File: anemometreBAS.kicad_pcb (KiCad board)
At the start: 2 copper layers, 1 part

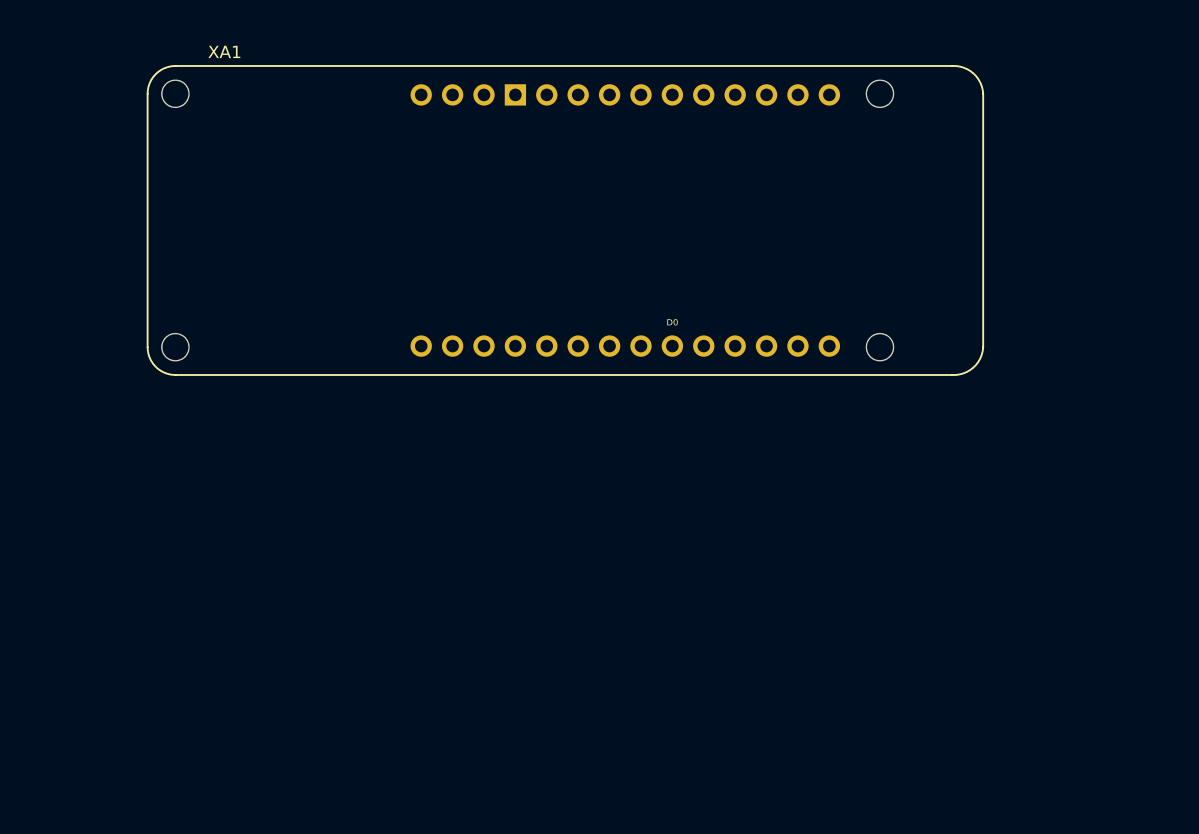
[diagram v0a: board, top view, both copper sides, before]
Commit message: first pcb version with schematic footprint update
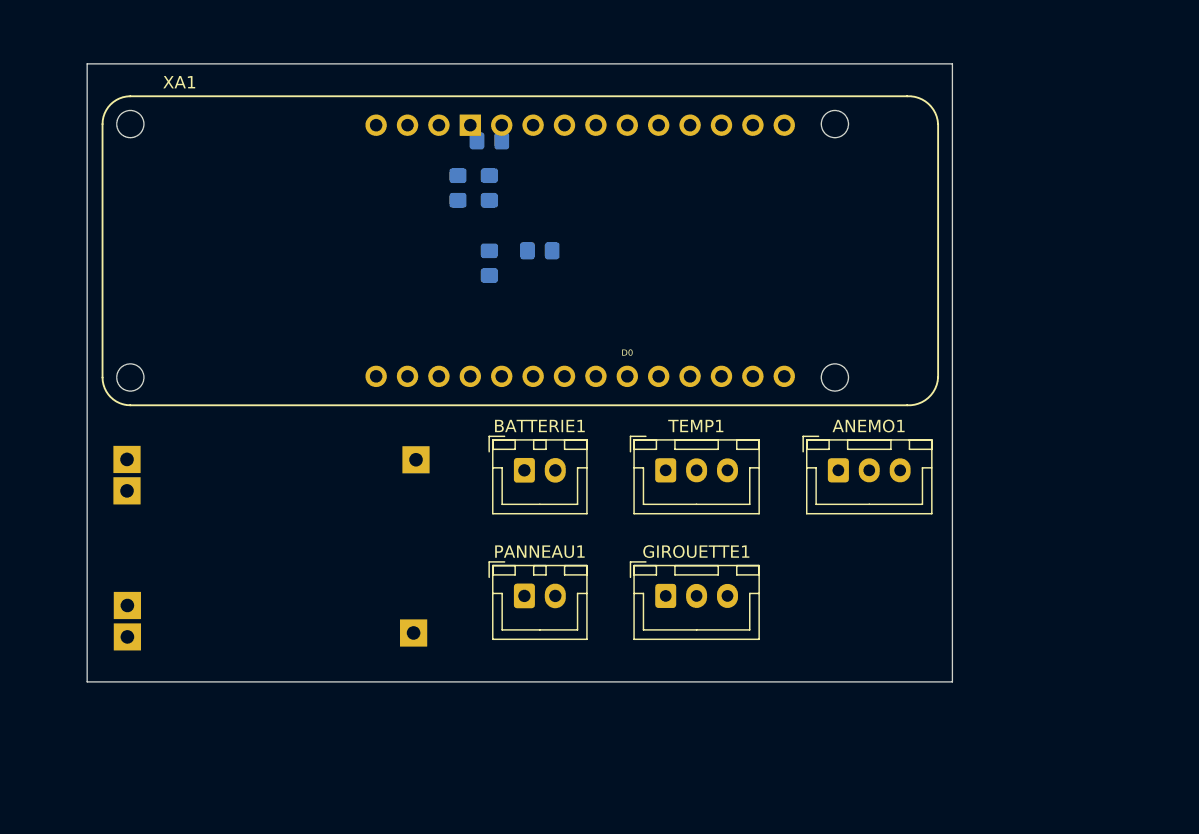
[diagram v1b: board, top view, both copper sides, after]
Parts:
- added ANEMO1: Conn_01x02_Male, Connector_JST:JST_XH_B3B-XH-A_1x03_P2.50mm_Vertical, F.Cu at (157.8, 88.9)
- added BATTERIE1: Conn_01x02_Male, Connector_JST:JST_XH_B2B-XH-A_1x02_P2.50mm_Vertical, F.Cu at (132.4, 88.9)
- added GIROUETTE1: Conn_01x02_Male, Connector_JST:JST_XH_B3B-XH-A_1x03_P2.50mm_Vertical, F.Cu at (143.8, 99.0)
- added PANNEAU1: Conn_01x02_Male, Connector_JST:JST_XH_B2B-XH-A_1x02_P2.50mm_Vertical, F.Cu at (132.4, 99.0)
- added R1: 4.7K, Resistor_SMD:R_0805_2012Metric_Pad1.20x1.40mm_HandSolder, B.Cu at (129.5, 72.1)
- added R2: 10K, Resistor_SMD:R_0805_2012Metric_Pad1.20x1.40mm_HandSolder, B.Cu at (133.6, 71.1)
- added R3: 10K, Resistor_SMD:R_0805_2012Metric_Pad1.20x1.40mm_HandSolder, B.Cu at (129.5, 66.0)
- added R4: 1.5K, Resistor_SMD:R_0805_2012Metric_Pad1.20x1.40mm_HandSolder, B.Cu at (127.0, 66.0)
- added R5: 2.5K, Resistor_SMD:R_0805_2012Metric_Pad1.20x1.40mm_HandSolder, B.Cu at (129.5, 62.2)
- added TEMP1: Conn_01x03_Male, Connector_JST:JST_XH_B3B-XH-A_1x03_P2.50mm_Vertical, F.Cu at (143.8, 88.9)
- added U1: TP4056, TP4056:TP4056, B.Cu at (125.0, 103.6)
- moved XA1 4.39 mm to (100.5, 60.9)
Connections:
- XA1 pad 3V3: unconnected-(XA1-Pad3V3) -> 3V3
- XA1 pad 5V: unconnected-(XA1-Pad5V) -> 5V
- XA1 pad A1: unconnected-(XA1-PadA1) -> Net-(TEMP1-Pad1)
- XA1 pad A4: unconnected-(XA1-PadA4) -> VBridgeBat
- XA1 pad A6: unconnected-(XA1-PadA6) -> VBridgeDir
- XA1 pad D0: unconnected-(XA1-PadD0) -> Net-(ANEMO1-Pad2)
- XA1 pad GND: unconnected-(XA1-PadGND) -> GND
- XA1 pad VIN: unconnected-(XA1-PadVIN) -> VIN
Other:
- board outline added: 70 x 50 mm

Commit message: schematic 	GND at the same pin for each connector 	add M3 hole*3 connected to GND PCB 	first routing
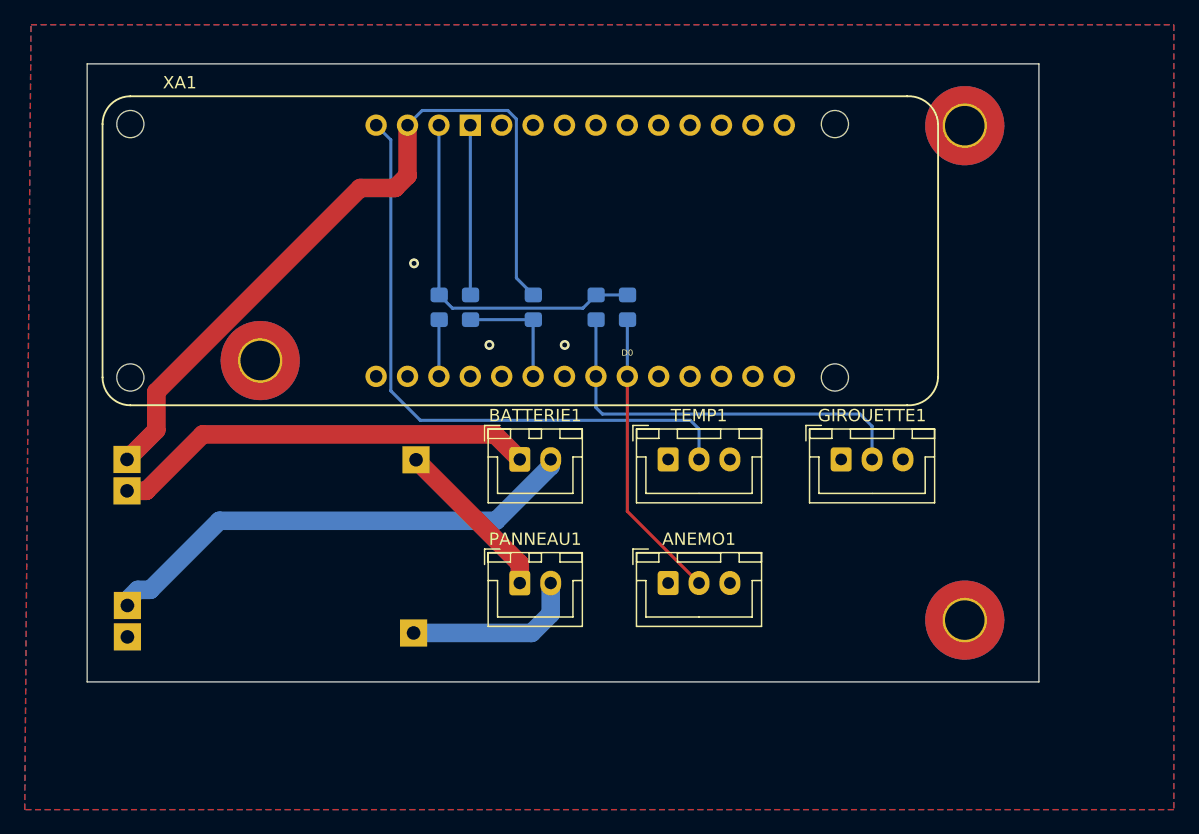
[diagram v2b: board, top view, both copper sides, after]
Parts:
- added H2: MountingHole_Pad, MountingHole:MountingHole_3.2mm_M3_Pad_TopBottom, F.Cu at (168.0, 101.0)
- added H3: MountingHole_Pad, MountingHole:MountingHole_3.2mm_M3_Pad_TopBottom, F.Cu at (168.0, 61.0)
- added H4: MountingHole_Pad, MountingHole:MountingHole_3.2mm_M3_Pad_TopBottom, F.Cu at (111.0, 80.0)
- moved GIROUETTE1 18.0 mm to (158.0, 88.0)
- moved ANEMO1 16.5 mm to (144.0, 98.0)
- moved R5 13.5 mm to (128.0, 75.7), turned to 90 degrees
- moved R3 13.0 mm to (138.2, 75.7)
- moved R4 11.4 mm to (133.1, 75.7)
- moved R2 8.44 mm to (140.7, 75.7), turned to 90 degrees
- moved R1 5.41 mm to (125.5, 75.7)
- moved PANNEAU1 1.11 mm to (132.0, 98.0)
- moved BATTERIE1 0.96 mm to (132.0, 88.0)
- moved TEMP1 0.90 mm to (144.0, 88.0)
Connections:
- GIROUETTE1 pad 1: VBridgeDir -> GND
- GIROUETTE1 pad 2: GND -> VBridgeDir
- R1 pad 2: Net-(TEMP1-Pad1) -> Net-(TEMP1-Pad3)
- TEMP1 pad 1: Net-(TEMP1-Pad1) -> GND
- TEMP1 pad 3: GND -> Net-(TEMP1-Pad3)
- XA1 pad A1: Net-(TEMP1-Pad1) -> Net-(TEMP1-Pad3)
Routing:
- net VIN: track 0.00 -> 62.5 mm
- net 5V: track 0.00 -> 50.7 mm
- net Net-(BATTERIE1-Pad2): track 0.00 -> 39.7 mm
- net Net-(BATTERIE1-Pad1): track 0.00 -> 34.5 mm
- net VBridgeDir: track 0.00 -> 33.5 mm
- net 3V3: track 0.00 -> 29.9 mm
- net Net-(ANEMO1-Pad2): track 0.00 -> 23.7 mm
- net Net-(PANNEAU1-Pad2): track 0.00 -> 14.2 mm
- net GND: track 0.00 -> 13.7 mm, vias 0 -> 3
- net Net-(PANNEAU1-Pad1): track 0.00 -> 13.5 mm
- net VBridgeBat: track 0.00 -> 9.68 mm
- net Net-(TEMP1-Pad3): track 0.00 -> 5.24 mm
- added copper zone on B.Cu, net GND
- added copper zone on F.Cu, net GND
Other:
- board size 70 x 50 mm -> 77 x 50 mm

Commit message: route temp sensor data change +5V net location change hole location drc ok only one error with hole under mkr processing board
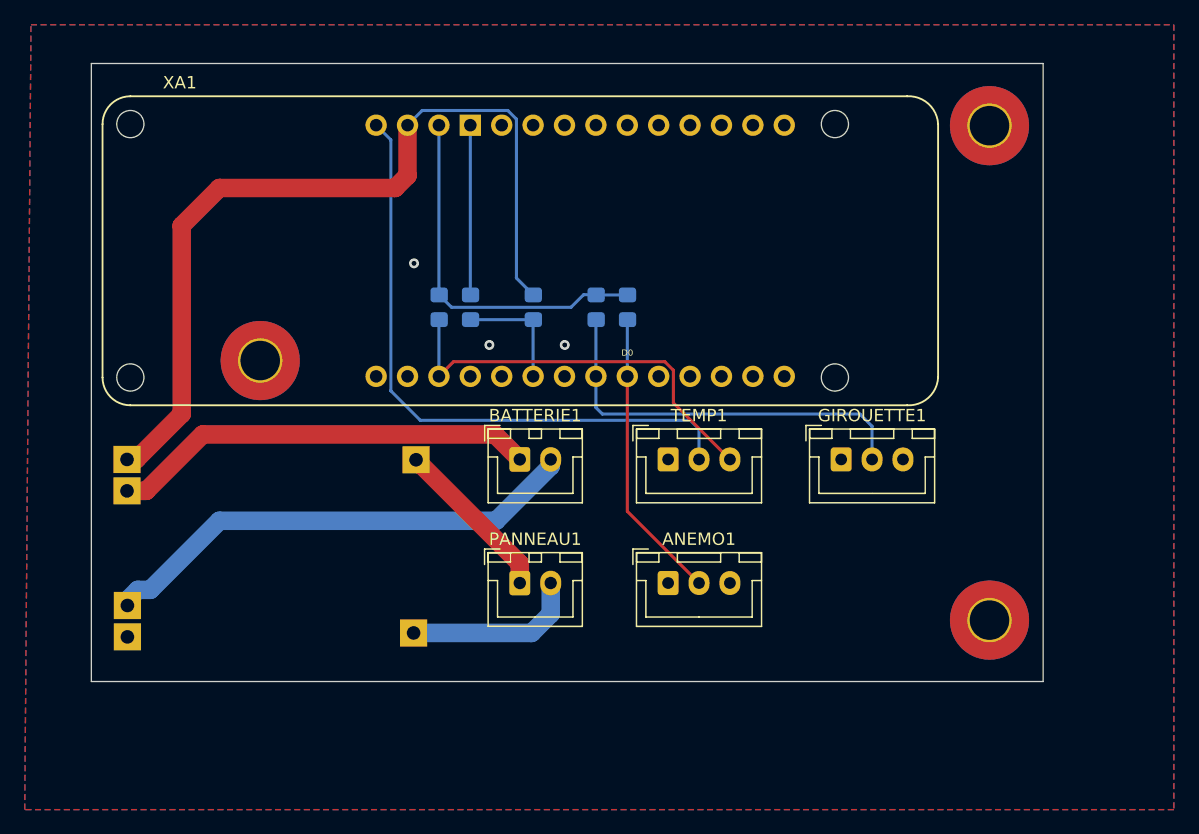
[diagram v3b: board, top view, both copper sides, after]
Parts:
- moved H2 2.00 mm to (170.0, 101.0)
- moved H3 2.00 mm to (170.0, 61.0)
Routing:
- net Net-(TEMP1-Pad3): track 5.24 -> 33.5 mm
- net VIN: track 62.5 -> 69.6 mm
- net VBridgeDir: track 33.5 -> 32.8 mm
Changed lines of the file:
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@@
   )
   (footprint "MountingHole:MountingHole_3.2mm_M3_Pad_TopBottom" (layer "F.Cu")
-    (at 168 61)
+    (at 170 61)
     (descr "Mounting Hole 3.2mm, M3")
     (tags "mounting hole 3.2mm m3")
@@
   )
   (footprint "MountingHole:MountingHole_3.2mm_M3_Pad_TopBottom" (layer "F.Cu")
-    (at 168 101)
+    (at 170 101)
     (descr "Mounting Hole 3.2mm, M3")
     (tags "mounting hole 3.2mm m3")
@@
       (net 9 "GND") (pinfunction "OUT-") (pintype "output"))
   )
-  (gr_line (start 97 56) (end 174 56) (layer "Edge.Cuts") (width 0.1))
-  (gr_line (start 174 106) (end 174 56) (layer "Edge.Cuts") (width 0.1))
-  (gr_line (start 97 106) (end 97 56) (layer "Edge.Cuts") (width 0.1))
-  (gr_line (start 174 106) (end 97 106) (layer "Edge.Cuts") (width 0.1))
-  (dimension (type aligned) (layer "Edge.Cuts")
-    (pts (xy 174 56) (xy 174 106))
+  (gr_line (start 97.3392 55.9688) (end 174.3392 55.9688) (layer "Edge.Cuts") (width 0.1))
+  (gr_line (start 174.3392 105.9688) (end 174.3392 55.9688) (layer "Edge.Cuts") (width 0.1))
+  (gr_line (start 97.3392 105.9688) (end 97.3392 55.9688) (layer "Edge.Cuts") (width 0.1))
+  (gr_line (start 174.3392 105.9688) (end 97.3392 105.9688) (layer "Edge.Cuts") (width 0.1))
+  (dimension (type aligned) (layer "Cmts.User")
+    (pts (xy 174.3392 55.9688) (xy 174.3392 105.9688))
     (height -8.89)
-    (gr_text "50,0000 mm" (at 181.74 81 90) (layer "Edge.Cuts")
+    (gr_text "50,0000 mm" (at 182.0792 80.9688 90) (layer "Cmts.User")
       (effects (font (size 1 1) (thickness 0.15)))
     )
@@
     (style (thickness 0.1) (arrow_length 1.27) (text_position_mode 0) (extension_height 0.58642) (extension_offset 0.5) keep_text_aligned)
   )
-  (dimension (type aligned) (layer "Edge.Cuts")
-    (pts (xy 174 106) (xy 97 106))
+  (dimension (type aligned) (layer "Cmts.User")
+    (pts (xy 174.3392 105.9688) (xy 97.3392 105.9688))
     (height -6.35)
-    (gr_text "77,0000 mm" (at 135.5 111.2) (layer "Edge.Cuts")
+    (gr_text "77,0000 mm" (at 135.8392 111.1688) (layer "Cmts.User")
       (effects (font (size 1 1) (thickness 0.15)))
     )
@@
   )
   (segment (start 125.4578 74.6738) (end 125.476 74.692) (width 0.25) (layer "B.Cu") (net 1))
-  (segment (start 137.10052 75.76748) (end 138.176 74.692) (width 0.25) (layer "B.Cu") (net 1))
-  (segment (start 137.668 74.692) (end 137.684 74.708) (width 0.25) (layer "B.Cu") (net 1))
-  (segment (start 125.476 74.692) (end 126.55148 75.76748) (width 0.25) (layer "B.Cu") (net 1))
+  (segment (start 136.144 75.692) (end 126.476 75.692) (width 0.25) (layer "B.Cu") (net 1))
+  (segment (start 137.16 74.676) (end 136.144 75.692) (width 0.25) (layer "B.Cu") (net 1))
+  (segment (start 126.476 75.692) (end 125.476 74.692) (width 0.25) (layer "B.Cu") (net 1))
   (segment (start 125.476 74.708) (end 125.4578 74.6898) (width 0.25) (layer "B.Cu") (net 1))
+  (segment (start 138.176 74.692) (end 138.16 74.676) (width 0.25) (layer "B.Cu") (net 1))
   (segment (start 125.4578 60.96) (end 125.4578 74.6738) (width 0.25) (layer "B.Cu") (net 1))
+  (segment (start 138.16 74.676) (end 137.16 74.676) (width 0.25) (layer "B.Cu") (net 1))
   (segment (start 140.716 74.692) (end 138.176 74.692) (width 0.25) (layer "B.Cu") (net 1))
-  (segment (start 126.55148 75.76748) (end 137.10052 75.76748) (width 0.25) (layer "B.Cu") (net 1))
-  (segment (start 102.592521 85.635189) (end 102.592521 82.539183) (width 1.5) (layer "F.Cu") (net 5))
-  (segment (start 102.592521 82.539183) (end 119.091704 66.04) (width 1.5) (layer "F.Cu") (net 5))
-  (segment (start 119.091704 66.04) (end 121.92 66.04) (width 1.5) (layer "F.Cu") (net 5))
-  (segment (start 121.92 66.04) (end 122.9178 65.0422) (width 1.5) (layer "F.Cu") (net 5))
-  (segment (start 122.9178 65.0422) (end 122.9178 60.96) (width 1.5) (layer "F.Cu") (net 5))
-  (segment (start 100.224054 88.003656) (end 102.592521 85.635189) (width 1.5) (layer "F.Cu") (net 5))
+  (segment (start 122.9178 60.96) (end 122.9178 65.0422) (width 1.5) (layer "F.Cu") (net 5))
+  (segment (start 104.648 84.328) (end 100.972344 88.003656) (width 1.5) (layer "F.Cu") (net 5))
+  (segment (start 100.972344 88.003656) (end 100.224054 88.003656) (width 1.5) (layer "F.Cu") (net 5))
+  (segment (start 122.9178 65.0422) (end 121.92 66.04) (width 1.5) (layer "F.Cu") (net 5))
+  (segment (start 121.92 66.04) (end 107.696 66.04) (width 1.5) (layer "F.Cu") (net 5))
+  (segment (start 107.696 66.04) (end 104.648 69.088) (width 1.5) (layer "F.Cu") (net 5))
+  (segment (start 104.648 69.088) (end 104.648 84.328) (width 1.5) (layer "F.Cu") (net 5))
   (segment (start 131.725911 73.321911) (end 131.725911 60.467867) (width 0.25) (layer "B.Cu") (net 5))
   (segment (start 124.105911 59.771889) (end 122.9178 60.96) (width 0.25) (layer "B.Cu") (net 5))
@@
   (segment (start 159.512 84.328) (end 138.684 84.328) (width 0.25) (layer "B.Cu") (net 26))
   (segment (start 160.5 85.316) (end 159.512 84.328) (width 0.25) (layer "B.Cu") (net 26))
-  (segment (start 137.668 76.692) (end 138.1578 77.1818) (width 0.25) (layer "B.Cu") (net 26))
   (segment (start 140.6978 92.1978) (end 140.6978 81.28) (width 0.25) (layer "F.Cu") (net 27))
   (segment (start 146.5 98) (end 140.6978 92.1978) (width 0.25) (layer "F.Cu") (net 27))
@@
   (segment (start 132.962 102.038) (end 123.409 102.038) (width 1.5) (layer "B.Cu") (net 31))
   (segment (start 134.5 98) (end 134.5 100.5) (width 1.5) (layer "B.Cu") (net 31))
+  (segment (start 143.729933 80.091889) (end 126.645911 80.091889) (width 0.25) (layer "F.Cu") (net 32))
+  (segment (start 149 88) (end 144.425911 83.425911) (width 0.25) (layer "F.Cu") (net 32))
+  (segment (start 144.425911 83.425911) (end 144.425911 80.787867) (width 0.25) (layer "F.Cu") (net 32))
+  (segment (start 144.425911 80.787867) (end 143.729933 80.091889) (width 0.25) (layer "F.Cu") (net 32))
+  (segment (start 126.645911 80.091889) (end 125.4578 81.28) (width 0.25) (layer "F.Cu") (net 32))
   (segment (start 125.4578 76.7102) (end 125.4578 81.28) (width 0.25) (layer "B.Cu") (net 32))
-  (segment (start 125.238507 81.060707) (end 125.4578 81.28) (width 0.25) (layer "B.Cu") (net 32))
   (segment (start 125.476 76.692) (end 125.4578 76.7102) (width 0.25) (layer "B.Cu") (net 32))
-  (segment (start 125.476 76.708) (end 125.238507 76.945493) (width 0.25) (layer "B.Cu") (net 32))
   (zone (net 9) (net_name "GND") (layers F&B.Cu) (hatch edge 0.508)
     (connect_pads (clearance 0.508))
